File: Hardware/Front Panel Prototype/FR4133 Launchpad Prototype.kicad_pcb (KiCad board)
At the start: 2 copper layers, 118.1 x 90.8 mm, 46 parts, among them J1 CONN_01X08, J2 CONN_01X08, J3 CONN_01X08, J5 CONN_01X08, J8 CONN_01X08, SW1 SW_Push, SW10 Rotary_Encoder_Switch, SW11 Rotary_Encoder_Switch, SW12 Rotary_Encoder_Switch, SW13 SW_DIP_x04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

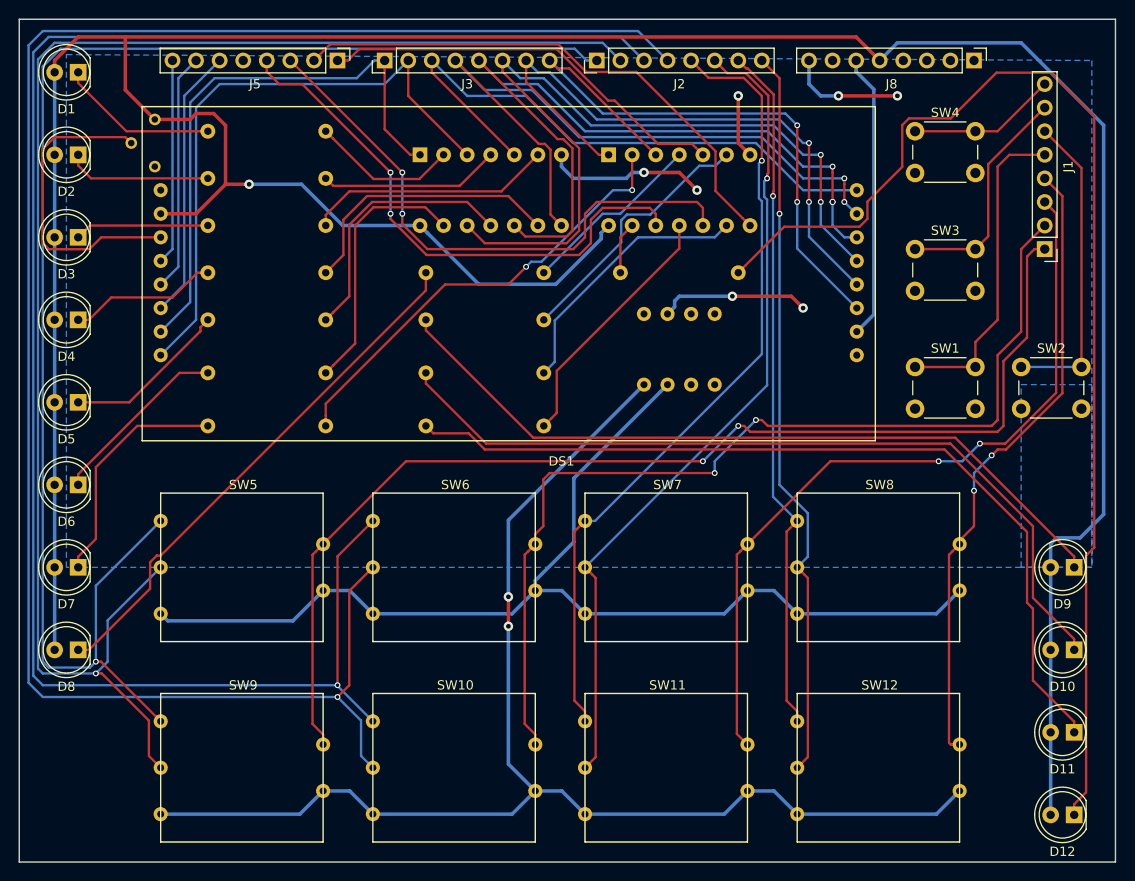
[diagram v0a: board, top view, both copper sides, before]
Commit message: fixed through hole sizes for LCD and encoders
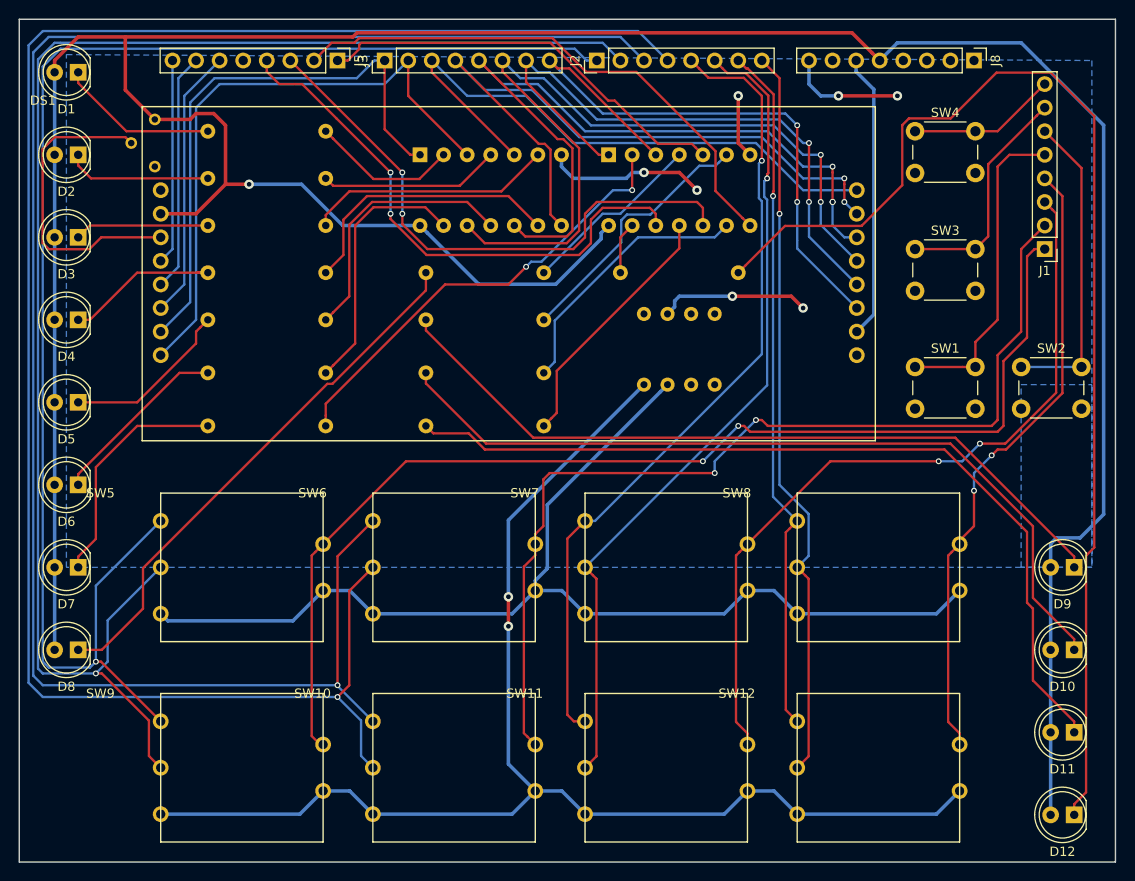
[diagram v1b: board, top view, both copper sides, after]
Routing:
- net /P2.4: track 86.3 -> 87.7 mm
- net Net-(D4-Pad1): track 16.1 -> 17.2 mm
- net Net-(D8-Pad1): track 57.1 -> 58.0 mm
- net /SN74_C: track 44.6 -> 45.4 mm
- net /SN74_D: track 58.3 -> 58.9 mm
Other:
- board text added: "The White Box Front Panel Proto Version 1.1"
